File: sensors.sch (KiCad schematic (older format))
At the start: 13 parts, among them U6 ICM-20948, U7 BMP388

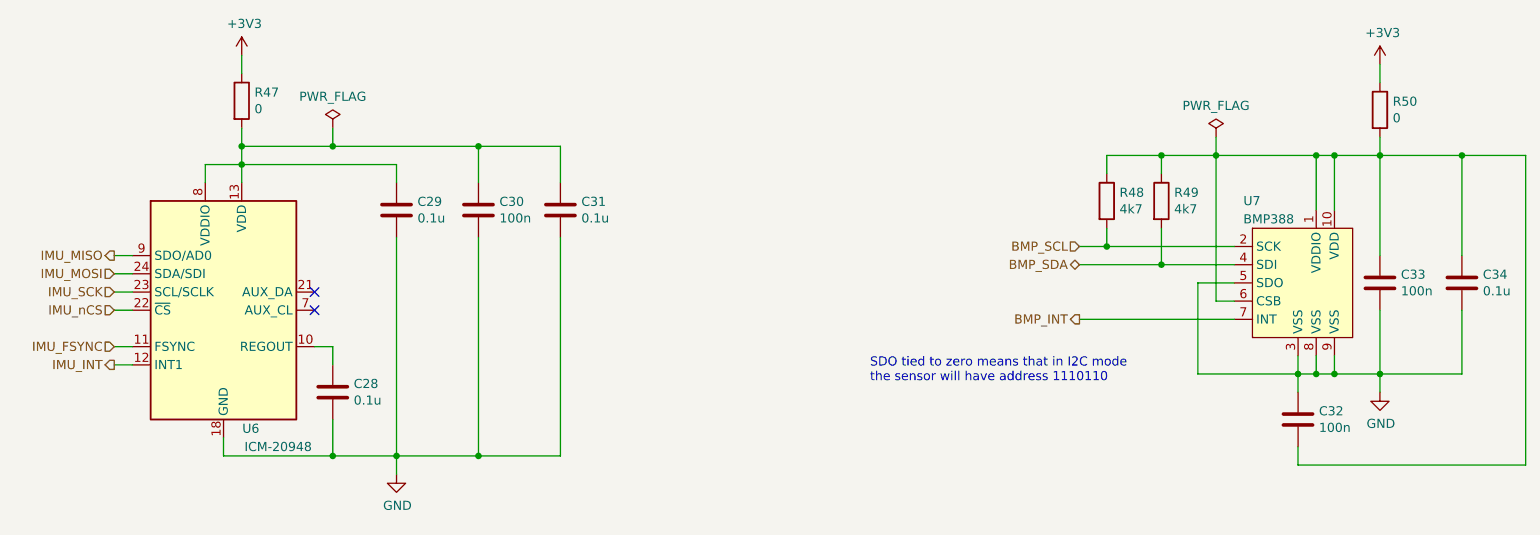
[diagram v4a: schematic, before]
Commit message: Re-annotated all elements
This is a step to prepare for a change from 0805 to 0603 components. Not
critical but nice to have them in order.
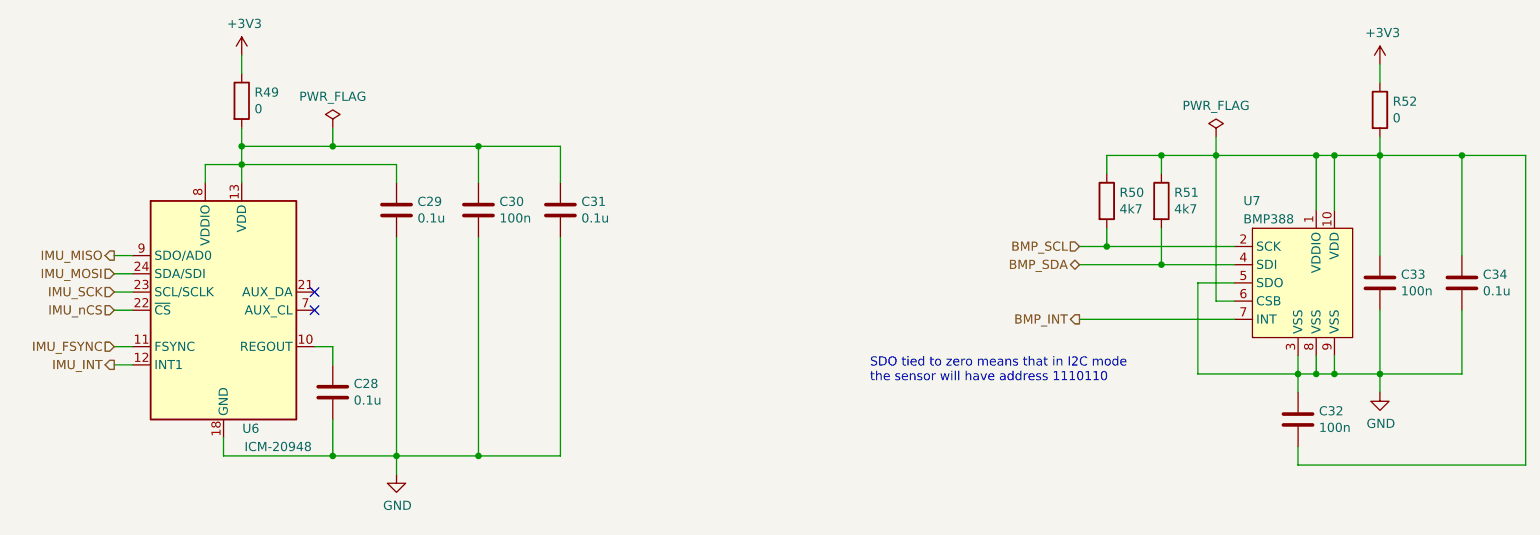
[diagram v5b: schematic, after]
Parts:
- renumbered R47 to R49, R48 to R50, R49 to R51, R50 to R52
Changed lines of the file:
@@
 $EndComp
 $Comp
-L Device:R R49
+L Device:R R51
 U 1 1 5E4A4DD8
 P 7900 3050
-F 0 "R49" H 7970 3096 50  0000 L CNN
+F 0 "R51" H 7970 3096 50  0000 L CNN
 F 1 "4k7" H 7970 3005 50  0000 L CNN
 F 2 "Resistor_SMD:R_0805_2012Metric_Pad1.15x1.40mm_HandSolder" V 7830 3050 50  0001 C CNN
@@
 $EndComp
 $Comp
-L Device:R R48
+L Device:R R50
 U 1 1 5E4A517E
 P 7600 3050
-F 0 "R48" H 7670 3096 50  0000 L CNN
+F 0 "R50" H 7670 3096 50  0000 L CNN
 F 1 "4k7" H 7670 3005 50  0000 L CNN
 F 2 "Resistor_SMD:R_0805_2012Metric_Pad1.15x1.40mm_HandSolder" V 7530 3050 50  0001 C CNN
@@
 Connection ~ 8650 4000
 $Comp
-L power:GND #PWR063
+L power:GND #PWR061
 U 1 1 5E4AE342
 P 9100 4100
-F 0 "#PWR063" H 9100 3850 50  0001 C CNN
+F 0 "#PWR061" H 9100 3850 50  0001 C CNN
 F 1 "GND" H 9105 3927 50  0000 C CNN
 F 2 "" H 9100 4100 50  0001 C CNN
@@
 Connection ~ 9100 4000
 $Comp
-L power:+3V3 #PWR062
+L power:+3V3 #PWR060
 U 1 1 5E4B6048
 P 9100 2300
-F 0 "#PWR062" H 9100 2150 50  0001 C CNN
+F 0 "#PWR060" H 9100 2150 50  0001 C CNN
 F 1 "+3V3" H 9115 2473 50  0000 C CNN
 F 2 "" H 9100 2300 50  0001 C CNN
@@
 	9100 4000 9100 4100
 $Comp
-L Device:R R50
+L Device:R R52
 U 1 1 5EC5840F
 P 9100 2550
-F 0 "R50" H 9170 2596 50  0000 L CNN
+F 0 "R52" H 9170 2596 50  0000 L CNN
 F 1 "0" H 9170 2505 50  0000 L CNN
 F 2 "Resistor_SMD:R_0805_2012Metric_Pad1.15x1.40mm_HandSolder" V 9030 2550 50  0001 C CNN
@@
 $EndComp
 $Comp
-L power:GND #PWR060
+L power:GND #PWR059
 U 1 1 5EC5DA97
 P 3700 4550
-F 0 "#PWR060" H 3700 4300 50  0001 C CNN
+F 0 "#PWR059" H 3700 4300 50  0001 C CNN
 F 1 "GND" H 3705 4377 50  0000 C CNN
 F 2 "" H 3700 4550 50  0001 C CNN
@@
 IMU_nCS
 $Comp
-L power:+3V3 #PWR059
+L power:+3V3 #PWR058
 U 1 1 5EC713A1
 P 2850 2250
-F 0 "#PWR059" H 2850 2100 50  0001 C CNN
+F 0 "#PWR058" H 2850 2100 50  0001 C CNN
 F 1 "+3V3" H 2865 2423 50  0000 C CNN
 F 2 "" H 2850 2250 50  0001 C CNN
@@
 $EndComp
 $Comp
-L Device:R R47
+L Device:R R49
 U 1 1 5EC713A7
 P 2850 2500
-F 0 "R47" H 2920 2546 50  0000 L CNN
+F 0 "R49" H 2920 2546 50  0000 L CNN
 F 1 "0" H 2920 2455 50  0000 L CNN
 F 2 "Resistor_SMD:R_0805_2012Metric_Pad1.15x1.40mm_HandSolder" V 2780 2500 50  0001 C CNN
@@
 	2150 3650 2250 3650
 $Comp
-L power:PWR_FLAG #FLG0106
+L power:PWR_FLAG #FLG07
 U 1 1 5E3AD934
 P 8200 2700
-F 0 "#FLG0106" H 8200 2775 50  0001 C CNN
+F 0 "#FLG07" H 8200 2775 50  0001 C CNN
 F 1 "PWR_FLAG" H 8200 2873 50  0000 C CNN
 F 2 "" H 8200 2700 50  0001 C CNN
@@
 $EndComp
 $Comp
-L power:PWR_FLAG #FLG0107
+L power:PWR_FLAG #FLG06
 U 1 1 5E3AF8FB
 P 3350 2650
-F 0 "#FLG0107" H 3350 2725 50  0001 C CNN
+F 0 "#FLG06" H 3350 2725 50  0001 C CNN
 F 1 "PWR_FLAG" H 3350 2823 50  0000 C CNN
 F 2 "" H 3350 2650 50  0001 C CNN

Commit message: Use 0603 components, on both sides, route header
This decision was due to the current placement overcrowded and to the
fact that successful routing on one side was uncertain.
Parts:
- C28, C29, C30, C31, C32, C33, C34: footprint Capacitor_SMD:C_0805_2012Metric_Pad1.15x1.40mm_HandSolder -> Capacitor_SMD:C_0603_1608Metric_Pad1.05x0.95mm_HandSolder
- R49, R50, R51, R52: footprint Resistor_SMD:R_0805_2012Metric_Pad1.15x1.40mm_HandSolder -> Resistor_SMD:R_0603_1608Metric_Pad1.05x0.95mm_HandSolder
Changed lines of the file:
@@
 F 0 "C32" H 8765 4296 50  0000 L CNN
 F 1 "100n" H 8765 4205 50  0000 L CNN
-F 2 "Capacitor_SMD:C_0805_2012Metric_Pad1.15x1.40mm_HandSolder" H 8688 4100 50  0001 C CNN
+F 2 "Capacitor_SMD:C_0603_1608Metric_Pad1.05x0.95mm_HandSolder" H 8688 4100 50  0001 C CNN
 F 3 "~" H 8650 4250 50  0001 C CNN
 	1    8650 4250
@@
 F 0 "C33" H 9215 3546 50  0000 L CNN
 F 1 "100n" H 9215 3455 50  0000 L CNN
-F 2 "Capacitor_SMD:C_0805_2012Metric_Pad1.15x1.40mm_HandSolder" H 9138 3350 50  0001 C CNN
+F 2 "Capacitor_SMD:C_0603_1608Metric_Pad1.05x0.95mm_HandSolder" H 9138 3350 50  0001 C CNN
 F 3 "~" H 9100 3500 50  0001 C CNN
 	1    9100 3500
@@
 F 0 "R51" H 7970 3096 50  0000 L CNN
 F 1 "4k7" H 7970 3005 50  0000 L CNN
-F 2 "Resistor_SMD:R_0805_2012Metric_Pad1.15x1.40mm_HandSolder" V 7830 3050 50  0001 C CNN
+F 2 "Resistor_SMD:R_0603_1608Metric_Pad1.05x0.95mm_HandSolder" V 7830 3050 50  0001 C CNN
 F 3 "~" H 7900 3050 50  0001 C CNN
 	1    7900 3050
@@
 F 0 "R50" H 7670 3096 50  0000 L CNN
 F 1 "4k7" H 7670 3005 50  0000 L CNN
-F 2 "Resistor_SMD:R_0805_2012Metric_Pad1.15x1.40mm_HandSolder" V 7530 3050 50  0001 C CNN
+F 2 "Resistor_SMD:R_0603_1608Metric_Pad1.05x0.95mm_HandSolder" V 7530 3050 50  0001 C CNN
 F 3 "~" H 7600 3050 50  0001 C CNN
 	1    7600 3050
@@
 F 0 "C34" H 9665 3546 50  0000 L CNN
 F 1 "0.1u" H 9665 3455 50  0000 L CNN
-F 2 "Capacitor_SMD:C_0805_2012Metric_Pad1.15x1.40mm_HandSolder" H 9588 3350 50  0001 C CNN
+F 2 "Capacitor_SMD:C_0603_1608Metric_Pad1.05x0.95mm_HandSolder" H 9588 3350 50  0001 C CNN
 F 3 "~" H 9550 3500 50  0001 C CNN
 	1    9550 3500
@@
 F 0 "R52" H 9170 2596 50  0000 L CNN
 F 1 "0" H 9170 2505 50  0000 L CNN
-F 2 "Resistor_SMD:R_0805_2012Metric_Pad1.15x1.40mm_HandSolder" V 9030 2550 50  0001 C CNN
+F 2 "Resistor_SMD:R_0603_1608Metric_Pad1.05x0.95mm_HandSolder" V 9030 2550 50  0001 C CNN
 F 3 "~" H 9100 2550 50  0001 C CNN
 	1    9100 2550
@@
 F 0 "C30" H 4265 3146 50  0000 L CNN
 F 1 "100n" H 4265 3055 50  0000 L CNN
-F 2 "Capacitor_SMD:C_0805_2012Metric_Pad1.15x1.40mm_HandSolder" H 4188 2950 50  0001 C CNN
+F 2 "Capacitor_SMD:C_0603_1608Metric_Pad1.05x0.95mm_HandSolder" H 4188 2950 50  0001 C CNN
 F 3 "~" H 4150 3100 50  0001 C CNN
 	1    4150 3100
@@
 F 0 "C31" H 4715 3146 50  0000 L CNN
 F 1 "0.1u" H 4715 3055 50  0000 L CNN
-F 2 "Capacitor_SMD:C_0805_2012Metric_Pad1.15x1.40mm_HandSolder" H 4638 2950 50  0001 C CNN
+F 2 "Capacitor_SMD:C_0603_1608Metric_Pad1.05x0.95mm_HandSolder" H 4638 2950 50  0001 C CNN
 F 3 "~" H 4600 3100 50  0001 C CNN
 	1    4600 3100
@@
 F 0 "C29" H 3815 3146 50  0000 L CNN
 F 1 "0.1u" H 3815 3055 50  0000 L CNN
-F 2 "Capacitor_SMD:C_0805_2012Metric_Pad1.15x1.40mm_HandSolder" H 3738 2950 50  0001 C CNN
+F 2 "Capacitor_SMD:C_0603_1608Metric_Pad1.05x0.95mm_HandSolder" H 3738 2950 50  0001 C CNN
 F 3 "~" H 3700 3100 50  0001 C CNN
 	1    3700 3100
@@
 F 0 "C28" H 3465 4146 50  0000 L CNN
 F 1 "0.1u" H 3465 4055 50  0000 L CNN
-F 2 "Capacitor_SMD:C_0805_2012Metric_Pad1.15x1.40mm_HandSolder" H 3388 3950 50  0001 C CNN
+F 2 "Capacitor_SMD:C_0603_1608Metric_Pad1.05x0.95mm_HandSolder" H 3388 3950 50  0001 C CNN
 F 3 "~" H 3350 4100 50  0001 C CNN
 	1    3350 4100
@@
 F 0 "R49" H 2920 2546 50  0000 L CNN
 F 1 "0" H 2920 2455 50  0000 L CNN
-F 2 "Resistor_SMD:R_0805_2012Metric_Pad1.15x1.40mm_HandSolder" V 2780 2500 50  0001 C CNN
+F 2 "Resistor_SMD:R_0603_1608Metric_Pad1.05x0.95mm_HandSolder" V 2780 2500 50  0001 C CNN
 F 3 "~" H 2850 2500 50  0001 C CNN
 	1    2850 2500

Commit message: Placed everything apart from FTDI
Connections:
- net +3V3: no longer R49.1
- new net +1V8: R49.1
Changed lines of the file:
@@
 IMU_nCS
-$Comp
-L power:+3V3 #PWR058
-U 1 1 5EC713A1
-P 2850 2250
-F 0 "#PWR058" H 2850 2100 50  0001 C CNN
-F 1 "+3V3" H 2865 2423 50  0000 C CNN
-F 2 "" H 2850 2250 50  0001 C CNN
-F 3 "" H 2850 2250 50  0001 C CNN
-	1    2850 2250
-	1    0    0    -1
-$EndComp
 $Comp
 L Device:R R49
@@
 Wire Wire Line
 	8200 2700 8200 2800
+$Comp
+L power:+1V8 #PWR?
+U 1 1 5E7177C3
+P 2850 2250
+F 0 "#PWR?" H 2850 2100 50  0001 C CNN
+F 1 "+1V8" H 2865 2423 50  0000 C CNN
+F 2 "" H 2850 2250 50  0001 C CNN
+F 3 "" H 2850 2250 50  0001 C CNN
+	1    2850 2250
+	1    0    0    -1
+$EndComp
 $EndSCHEMATC
